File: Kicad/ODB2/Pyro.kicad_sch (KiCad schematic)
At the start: 38 parts

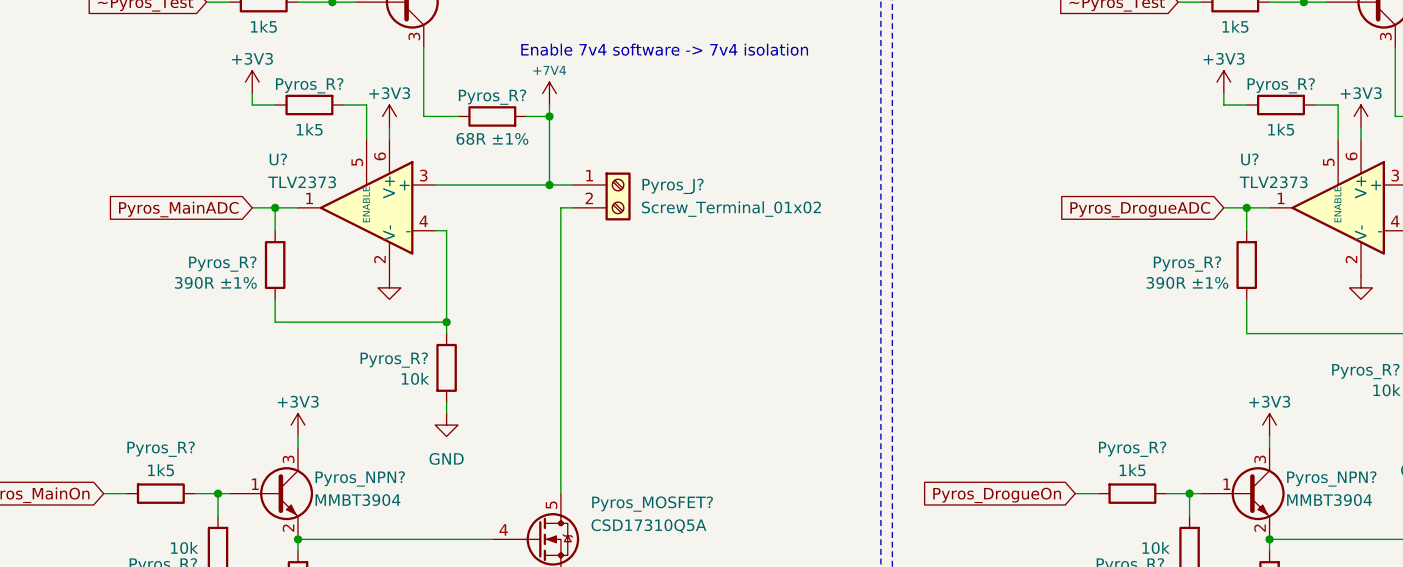
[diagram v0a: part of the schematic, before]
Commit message: fixed r value
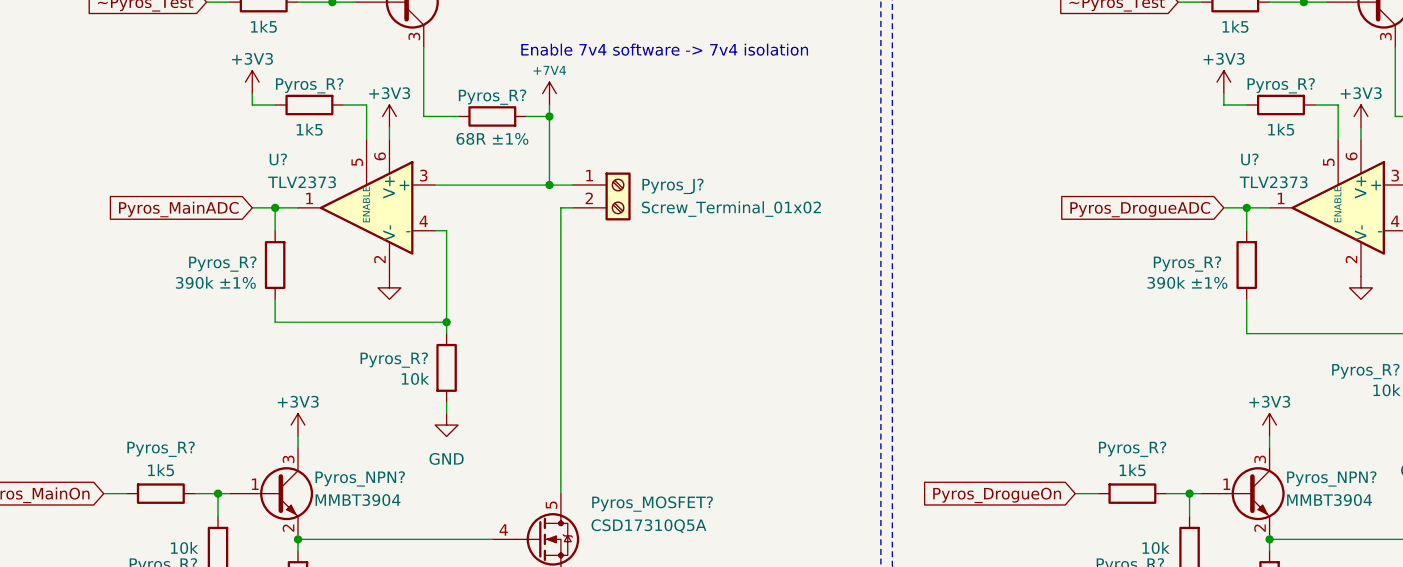
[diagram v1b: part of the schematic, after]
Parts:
- Pyros_R? (x2): value 390R ±1% -> 390k ±1%
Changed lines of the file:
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@@
 			)
 		)
-		(property "Value" "390R ±1%"
+		(property "Value" "390k ±1%"
 			(at 155.956 74.422 0)
 			(effects
@@
 			)
 		)
-		(property "Value" "390R ±1%"
+		(property "Value" "390k ±1%"
 			(at 48.006 74.422 0)
 			(effects

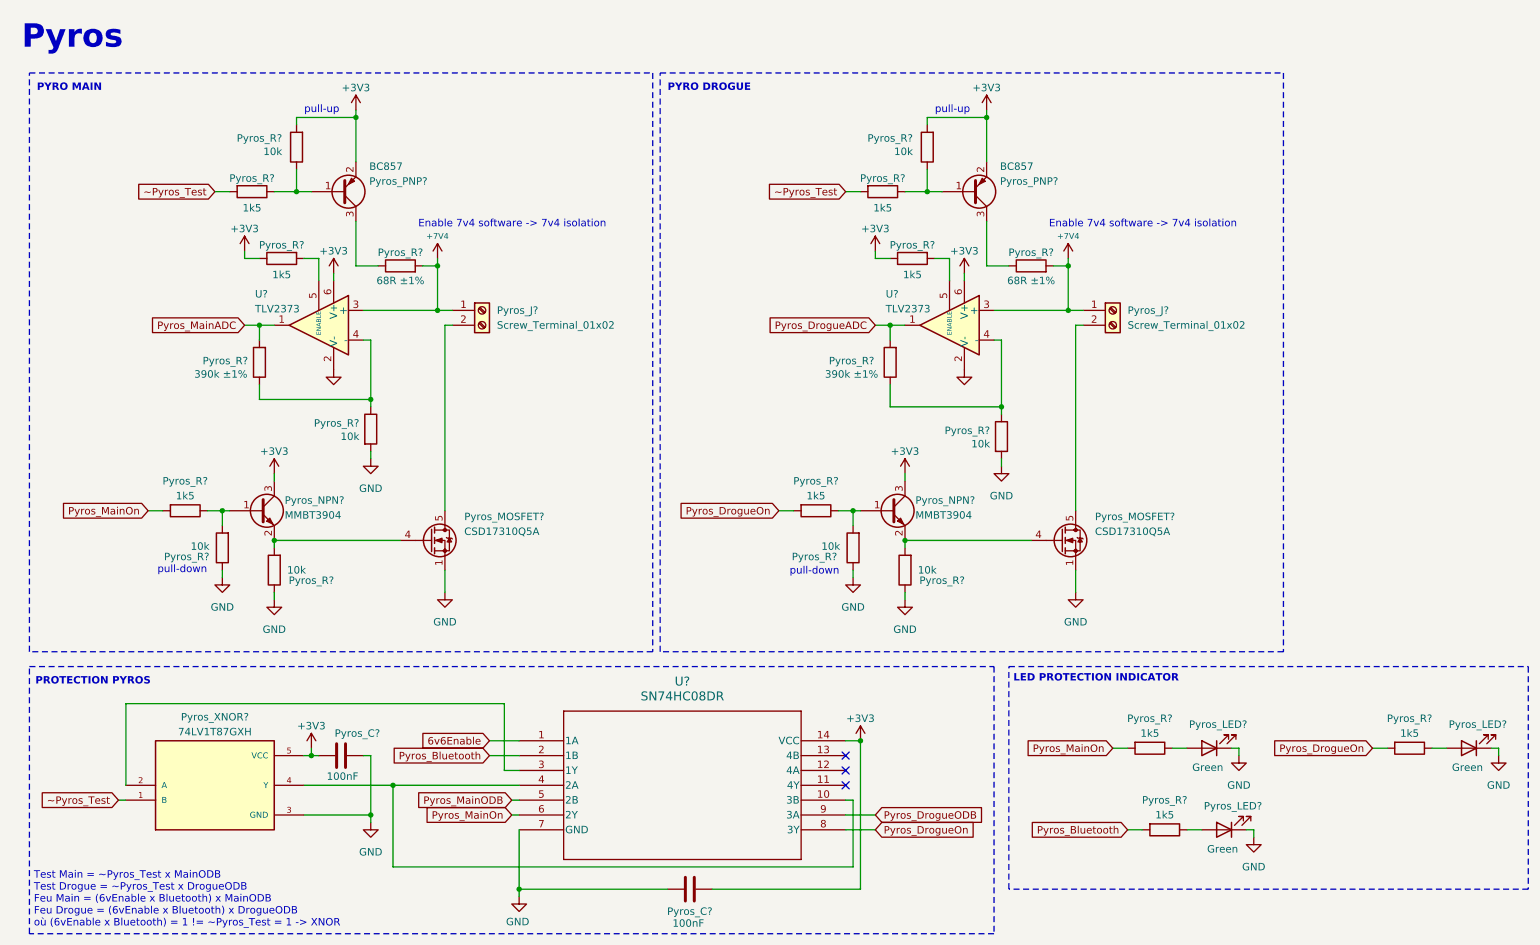
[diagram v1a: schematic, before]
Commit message: fix 3v3_R1 + amp pyros dual channel
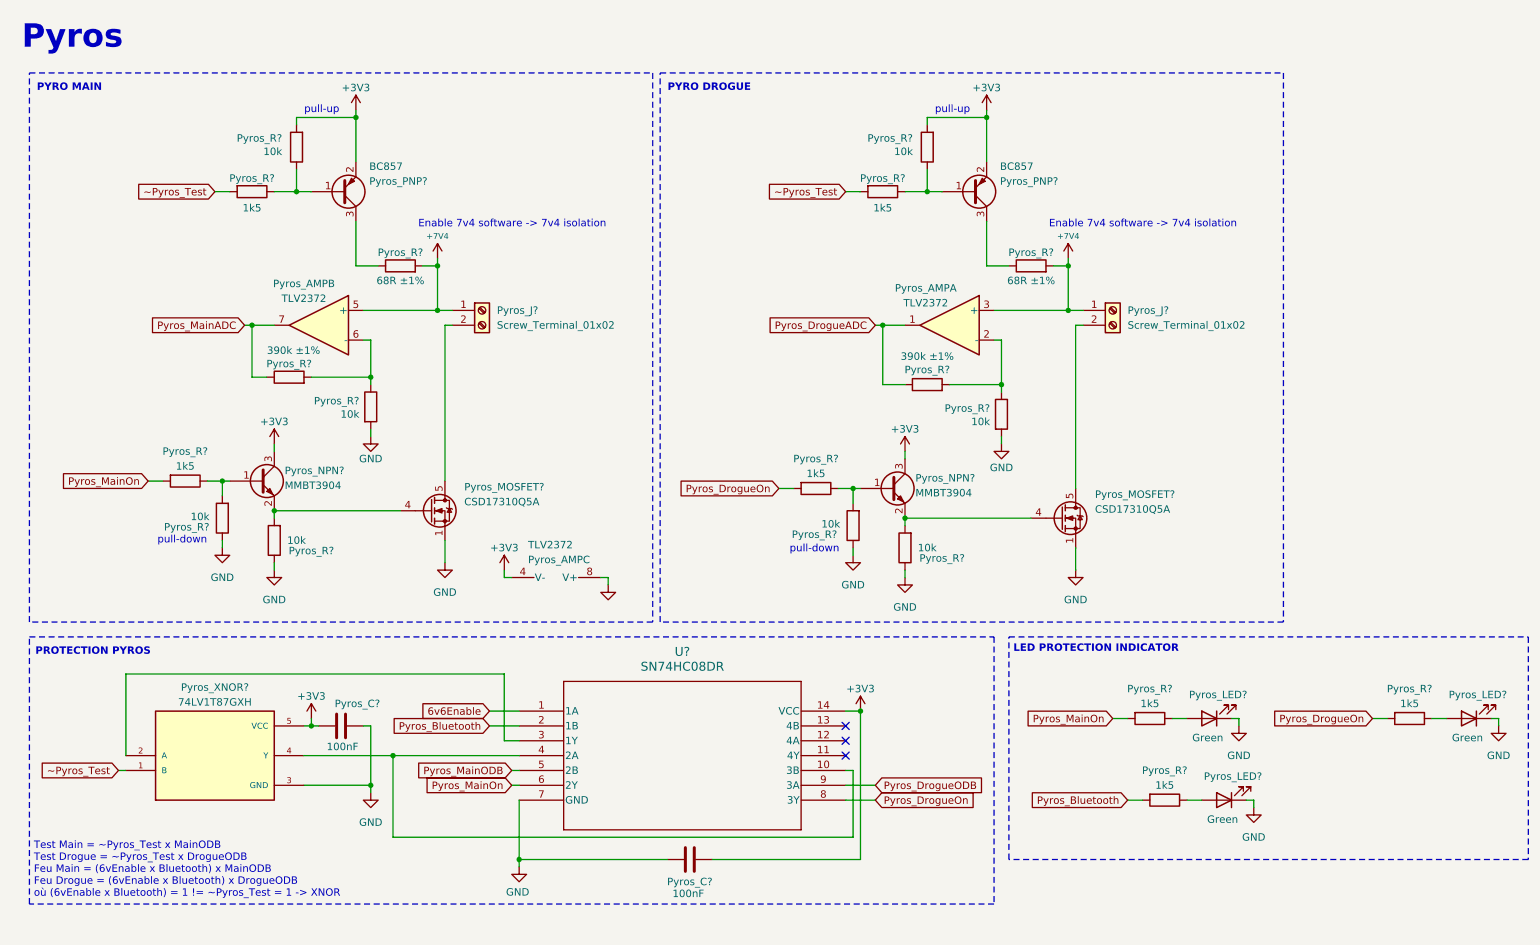
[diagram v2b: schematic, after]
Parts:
- removed Pyros_R? (x2): 1k5, Resistor_SMD:R_0805_2012Metric, symbol Device:R
- removed U? (x2): TLV2373, Package_TO_SOT_SMD:SOT-23-6, symbol Amplifier_Operational:OPA355NA
- added Pyros_AMP: TLV2372, symbol Amplifier_Operational:TLV2372
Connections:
- net +3V3: now also Pyros_AMP.4 (V-)
- net +7V4: now also Pyros_AMP.3 (+), Pyros_AMP.5 (+)
- net GND: now also Pyros_AMP.8 (V+)
- net Pyros_DrogueADC: now also Pyros_R?.1, Pyros_AMP.1; no longer Pyros_R?.2
- net Pyros_MainADC: now also Pyros_R?.1, Pyros_AMP.7; no longer Pyros_R?.2
- net at Pyros_R?.1: now also Pyros_R?.2, Pyros_AMP.2 (-); no longer Pyros_R?.1
- net at Pyros_R?.1: now also Pyros_R?.2, Pyros_AMP.6 (-); no longer Pyros_R?.1
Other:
- moved on the sheet: Pyros_C?, Pyros_LED?, Pyros_MOSFET?, Pyros_NPN?, Pyros_R?, Pyros_XNOR?, U?

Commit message: fix amp
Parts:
- Pyros_AMP1: renamed from Pyros_AMP; footprint (none) -> Package_SO:SOIC-8-1EP_3.9x4.9mm_P1.27mm_EP2.41x3.81mm
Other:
- note added: "Test Main = ~Pyros_Test x MainODB Test Drogue = ~Pyros_Test x DrogueODB Feu Main = (7v4Enable x Bluetooth) x MainODB Feu Drogue = (7v4Enable x Bluetooth) x DrogueODB où (7v4Enable x Bluetooth) = 1 != ~Pyros_Test = 1 -> XNOR"
- note removed: "Test Main = ~Pyros_Test x MainODB Test Drogue = ~Pyros_Test x DrogueODB Feu Main = (6vEnable x Bluetooth) x MainODB Feu Drogue = (6vEnable x Bluetooth) x DrogueODB où (6vEnable x Bluetooth) = 1 != ~Pyros_Test = 1 -> XNOR"
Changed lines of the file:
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@@
 		)
 	)
-	(text "Test Main = ~Pyros_Test x MainODB\nTest Drogue = ~Pyros_Test x DrogueODB\nFeu Main = (6vEnable x Bluetooth) x MainODB\nFeu Drogue = (6vEnable x Bluetooth) x DrogueODB\noù (6vEnable x Bluetooth) = 1 != ~Pyros_Test = 1 -> XNOR"
+	(text "Test Main = ~Pyros_Test x MainODB\nTest Drogue = ~Pyros_Test x DrogueODB\nFeu Main = (7v4Enable x Bluetooth) x MainODB\nFeu Drogue = (7v4Enable x Bluetooth) x DrogueODB\noù (7v4Enable x Bluetooth) = 1 != ~Pyros_Test = 1 -> XNOR"
 		(exclude_from_sim no)
 		(at 16.002 159.258 0)
@@
 		(on_board yes)
 		(dnp no)
-		(property "Reference" "Pyros_AMP"
+		(property "Reference" "Pyros_AMP1"
 			(at 100.584 106.172 90)
 			(effects
@@
 			)
 		)
-		(property "Footprint" ""
+		(property "Footprint" "Package_SO:SOIC-8-1EP_3.9x4.9mm_P1.27mm_EP2.41x3.81mm"
 			(at 105.41 106.68 0)
 			(effects
@@
 			(project ""
 				(path "/4b06c5d1-aa8b-48ed-8972-b43a60cfab78/8ab7427e-7183-4caa-ac8a-08b0bd412372"
-					(reference "Pyros_AMP")
+					(reference "Pyros_AMP1")
 					(unit 3)
 				)
@@
 		(dnp no)
 		(property "Reference" "Pyros_R?"
-			(at 175.768 80.264 0)
+			(at 175.006 80.264 0)
 			(effects
 				(font
@@
 		(on_board yes)
 		(dnp no)
-		(property "Reference" "#PWR077"
+		(property "Reference" "#PWR0105"
 			(at 85.09 58.42 0)
 			(effects
@@
 			(project "ODB2"
 				(path "/4b06c5d1-aa8b-48ed-8972-b43a60cfab78/8ab7427e-7183-4caa-ac8a-08b0bd412372"
-					(reference "#PWR077")
+					(reference "#PWR0105")
 					(unit 1)
 				)
@@
 		(on_board yes)
 		(dnp no)
-		(property "Reference" "Pyros_AMP"
+		(property "Reference" "Pyros_AMP1"
 			(at 168.656 59.69 0)
 			(effects
@@
 			)
 		)
-		(property "Footprint" ""
+		(property "Footprint" "Package_SO:SOIC-8-1EP_3.9x4.9mm_P1.27mm_EP2.41x3.81mm"
 			(at 172.72 66.04 0)
 			(effects
@@
 			(project ""
 				(path "/4b06c5d1-aa8b-48ed-8972-b43a60cfab78/8ab7427e-7183-4caa-ac8a-08b0bd412372"
-					(reference "Pyros_AMP")
+					(reference "Pyros_AMP1")
 					(unit 1)
 				)
@@
 		(on_board yes)
 		(dnp no)
-		(property "Reference" "Pyros_AMP"
+		(property "Reference" "Pyros_AMP1"
 			(at 62.23 58.928 0)
 			(effects
@@
 			)
 		)
-		(property "Footprint" ""
+		(property "Footprint" "Package_SO:SOIC-8-1EP_3.9x4.9mm_P1.27mm_EP2.41x3.81mm"
 			(at 64.77 66.04 0)
 			(effects
@@
 			(project ""
 				(path "/4b06c5d1-aa8b-48ed-8972-b43a60cfab78/8ab7427e-7183-4caa-ac8a-08b0bd412372"
-					(reference "Pyros_AMP")
+					(reference "Pyros_AMP1")
 					(unit 2)
 				)

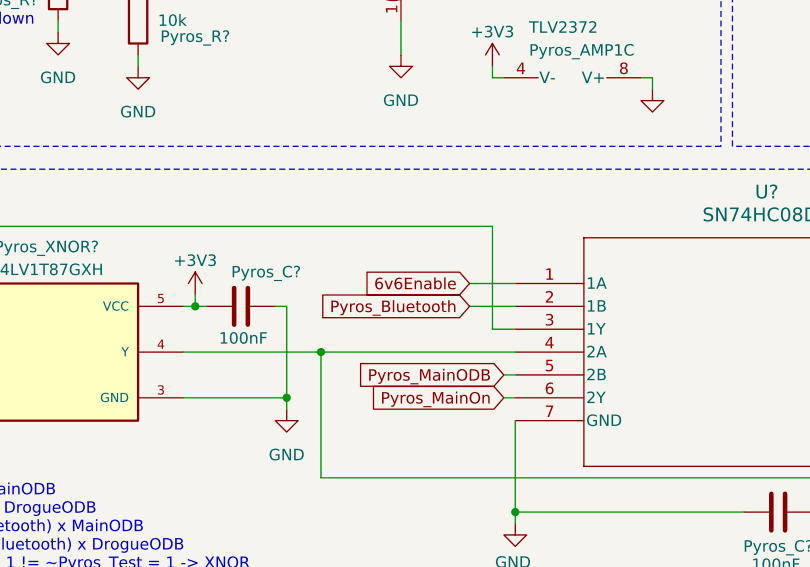
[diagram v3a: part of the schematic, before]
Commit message: Fix labels, 50 ohms, STM no connect
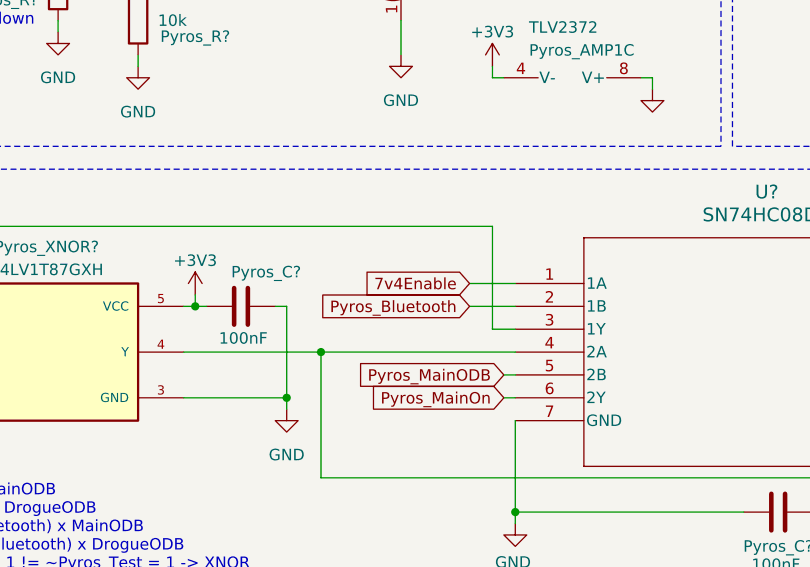
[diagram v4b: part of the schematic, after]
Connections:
- net 6v6Enable renamed 7v4Enable
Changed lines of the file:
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@@
 		)
 	)
-	(global_label "6v6Enable"
+	(global_label "7v4Enable"
 		(shape input)
 		(at 93.98 132.08 180)
